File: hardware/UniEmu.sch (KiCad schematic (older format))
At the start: 86 parts, among them J1 POWER, J8 JTAG, SW1 NCONF, SW3 USER, SW4 SW_DIP_x04, U1 TPS65251, U4 EP4CE6F17, U5 M25P40, X1 25MHz

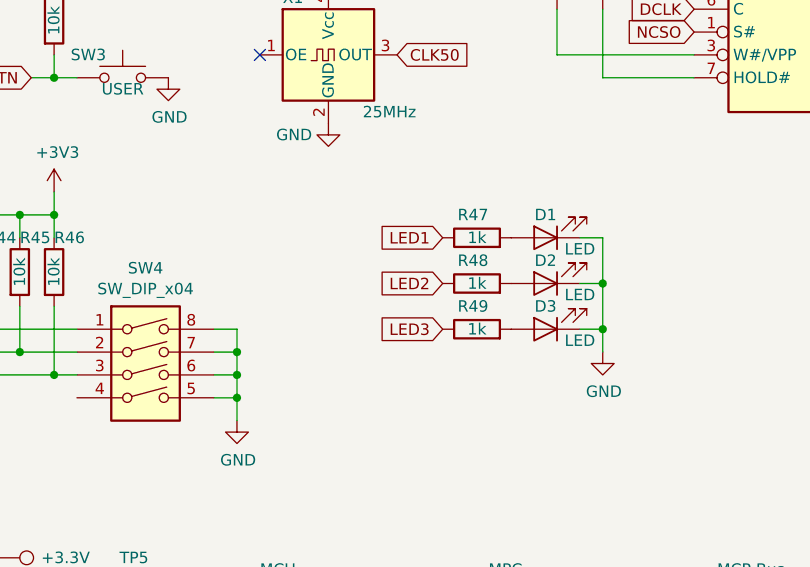
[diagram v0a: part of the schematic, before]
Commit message: Обновлена схема:
1. Исправлена нумерация CS SRAM;
2. Исправлена нумерация сигналов для светодиодов.
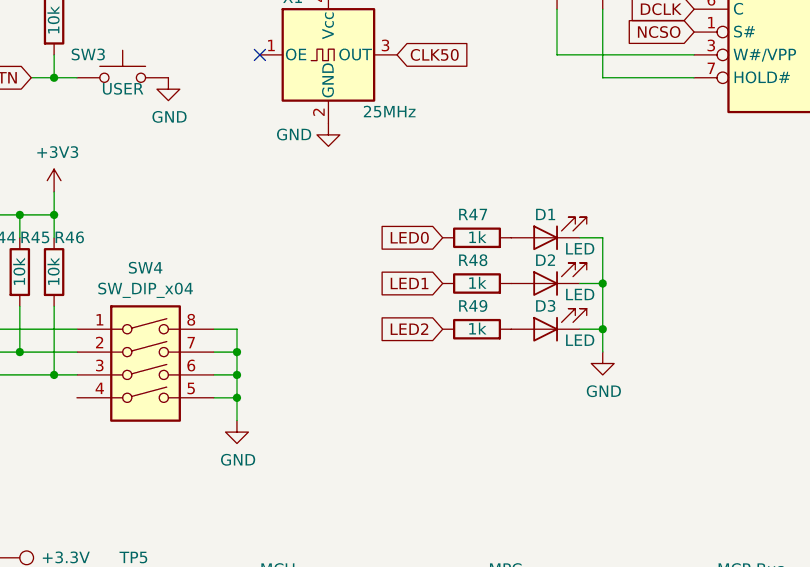
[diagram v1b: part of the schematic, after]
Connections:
- net LED3 is gone; now on net LED2: R49.1
- net LED1: now also R48.1; no longer R47.1
- net LED2: no longer R48.1
- new net LED0: R47.1
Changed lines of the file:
@@
 CLK50
 Text GLabel 7900 4400 0    50   Input ~ 0
+LED0
+Text GLabel 7900 4600 0    50   Input ~ 0
 LED1
-Text GLabel 7900 4600 0    50   Input ~ 0
+Text GLabel 7900 4800 0    50   Input ~ 0
 LED2
-Text GLabel 7900 4800 0    50   Input ~ 0
-LED3
 $Comp
 L Device:LED D1
